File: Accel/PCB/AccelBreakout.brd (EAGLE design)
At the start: 10.2 x 24.1 mm, 9 parts, among them U1 MMA8653FCR1

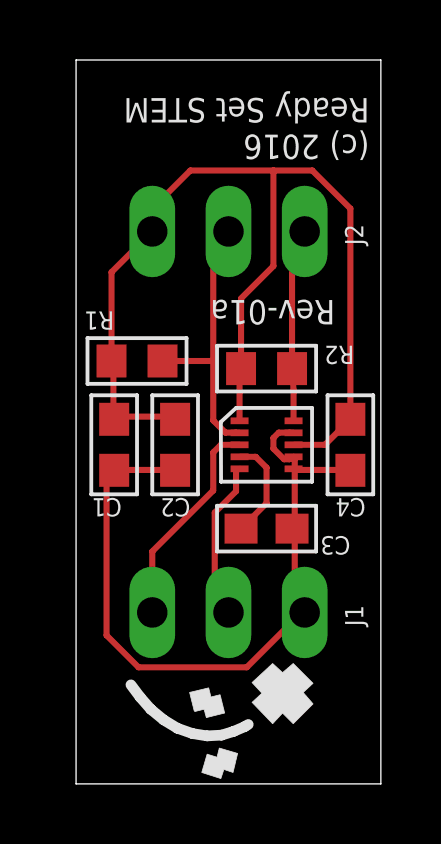
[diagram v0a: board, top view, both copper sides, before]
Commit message: added reverse voltage protection
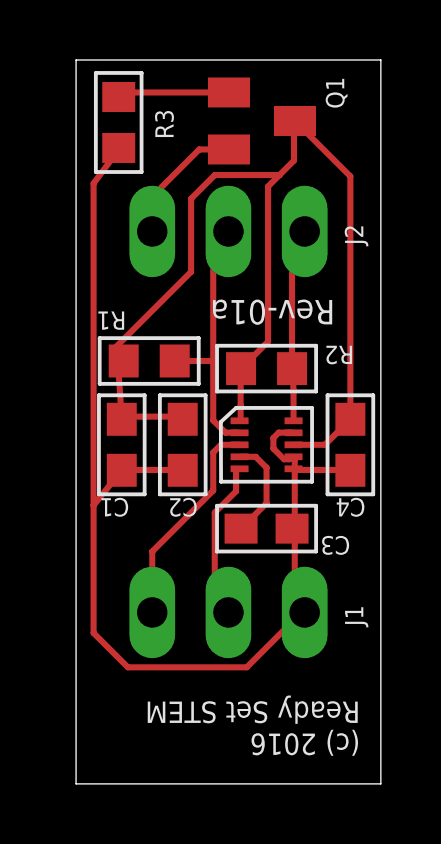
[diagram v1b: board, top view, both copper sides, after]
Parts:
- added Q1: MMBTA56-SOT23, transistor-pnp:SOT23
- added R3: 10K, AccelBreakout:R0603
- moved R1 0.41 mm to (2.44, 10.9)
- moved C1 0.25 mm to (1.52, 8.13)
- moved C2 0.25 mm to (3.56, 8.13)
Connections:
- new net N$1: J2.1, Q1.2
- new net N$2: Q1.1, R3.2
- net GND: now also R3.1
- net VCC: now also Q1.3; no longer J2.1
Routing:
- net GND: track 24.9 -> 38.1 mm
- net N$1: track 0.00 -> 4.42 mm
- net N$2: track 0.00 -> 3.90 mm
- net VCC: track 35.6 -> 39.0 mm
